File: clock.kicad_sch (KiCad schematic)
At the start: 10 parts

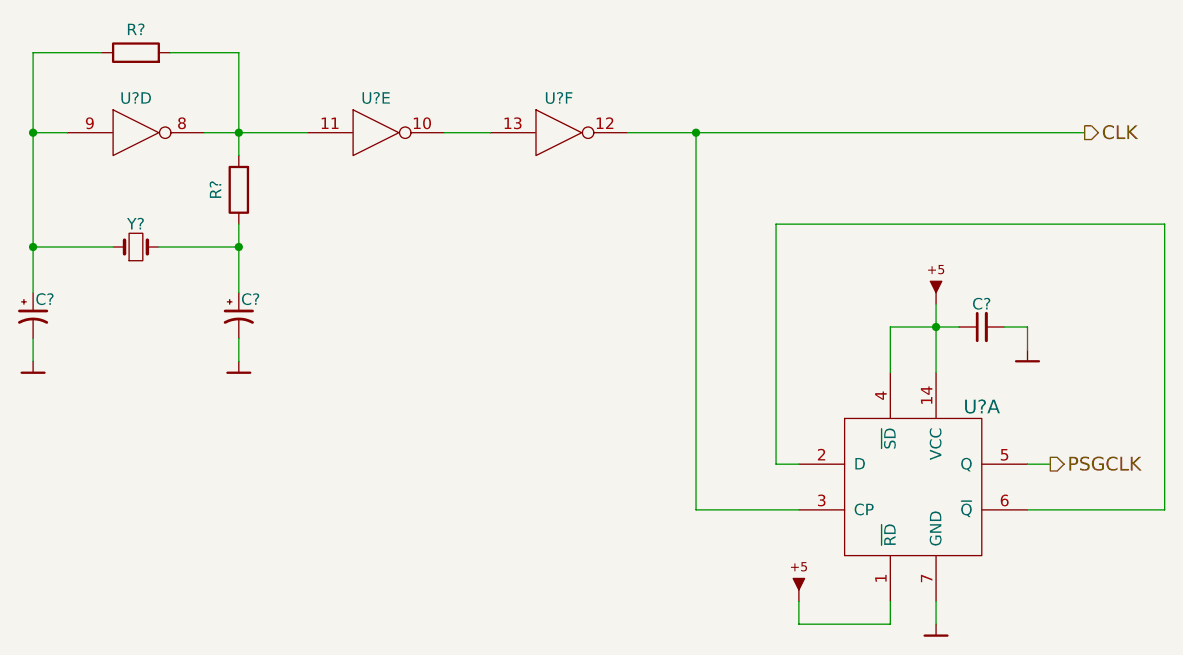
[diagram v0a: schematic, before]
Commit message: Implement power transform circuit
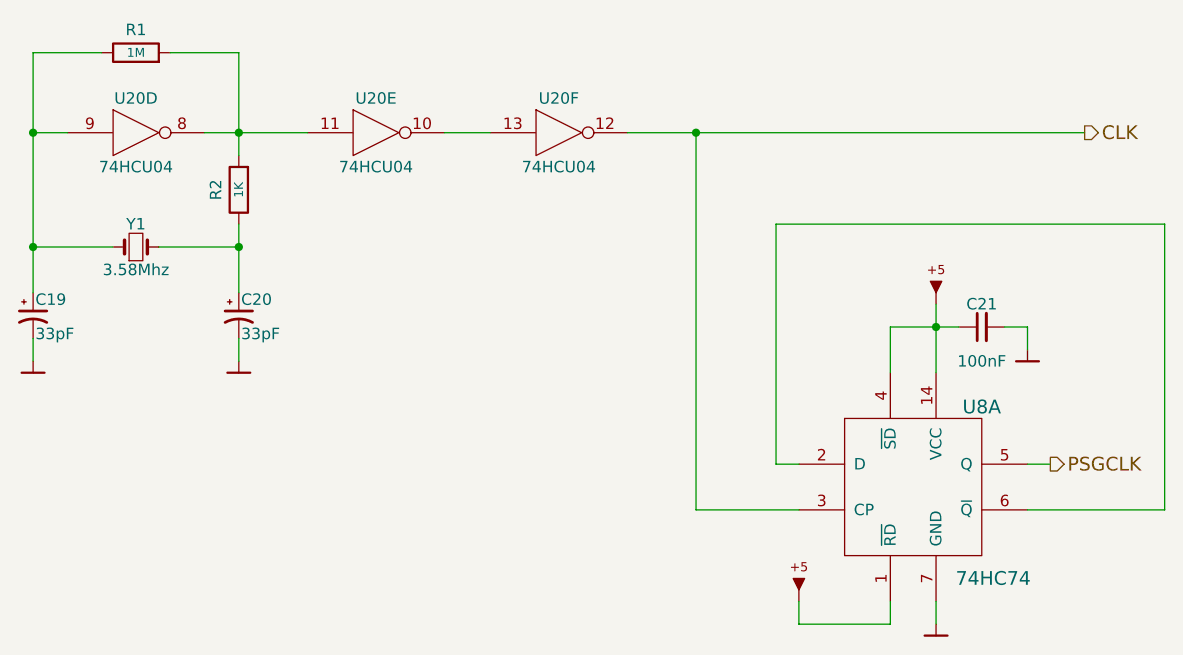
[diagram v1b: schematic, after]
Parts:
- C19, C20: renamed from C?; value (none) -> 33pF; footprint (none) -> artemisa:Disc_capacitor
- C21: renamed from C?; value (none) -> 100nF; footprint (none) -> artemisa:Disc_capacitor
- R1: renamed from R?; value (none) -> 1M; footprint (none) -> artemisa:Axial_resistor
- R2: renamed from R?; value (none) -> 1K; footprint (none) -> artemisa:Axial_resistor
- U20: renamed from U?; value (none) -> 74HCU04; footprint (none) -> artemisa:DIP-14_300
- U8: renamed from U?; value (none) -> 74HC74; footprint (none) -> artemisa:DIP-14_300
- Y1: renamed from Y?; value (none) -> 3.58Mhz; footprint (none) -> artemisa:Crystal
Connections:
- net VCC: now reaches U8.1 (~{RD})
- net VCC: now also C21.1, U8.14 (VCC), U8.4 (~{SD})
